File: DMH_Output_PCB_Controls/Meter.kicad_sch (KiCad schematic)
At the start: 63 parts, among them Q1 BC558, Q2 BC558, U1 TL072, U2 LM339, U3 LM339, U4 LM339, U5 LM339, U6 LM339

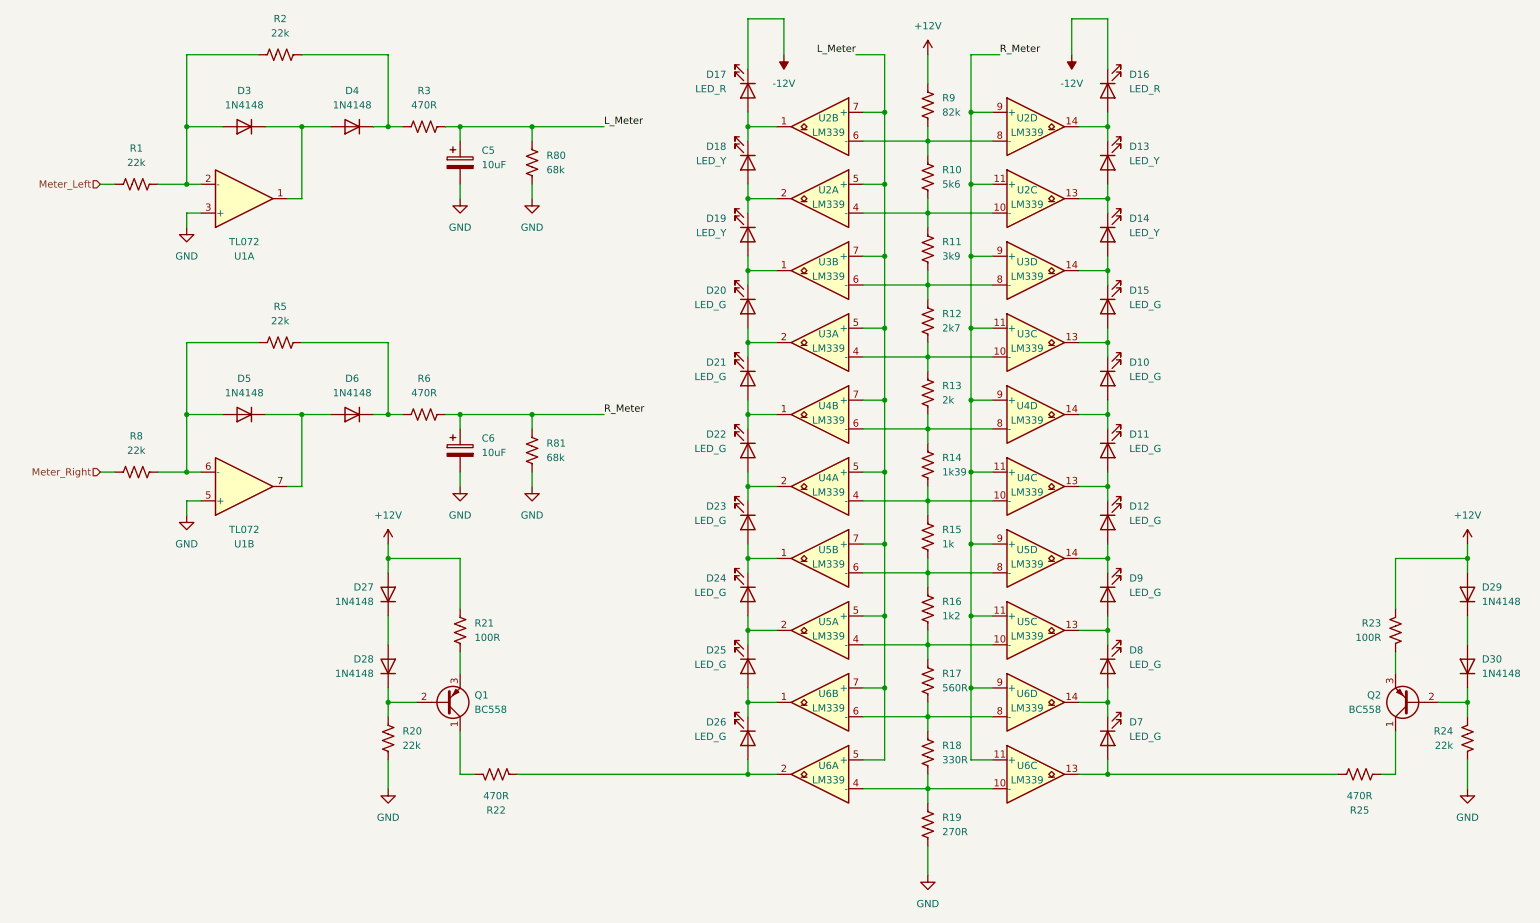
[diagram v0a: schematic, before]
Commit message: Starting design of Controls PCB
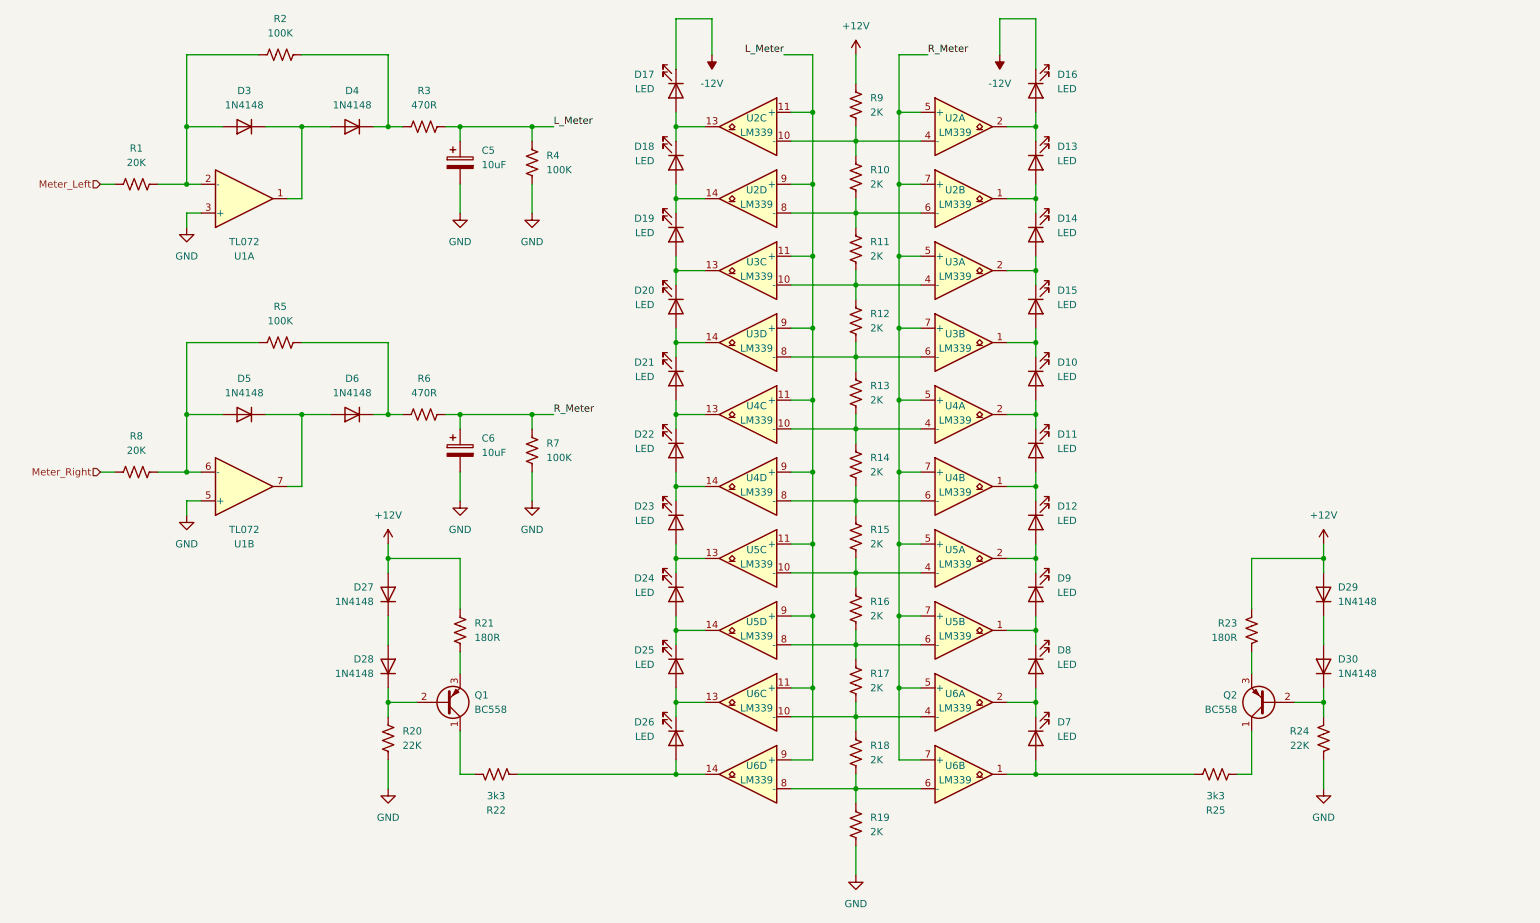
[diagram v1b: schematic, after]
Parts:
- removed R80: 68k, Resistor_THT:R_Axial_DIN0207_L6.3mm_D2.5mm_P7.62mm_Horizontal, symbol Device:R_US
- added R4: 100K, Resistor_THT:R_Axial_DIN0207_L6.3mm_D2.5mm_P7.62mm_Horizontal, symbol Device:R_US
- D10, D11, D12, D15, D20, D21, D22, D23, D24, D25, D26, D7, D8, D9: value LED_G -> LED
- D13, D14, D18, D19: value LED_Y -> LED
- D16, D17: value LED_R -> LED
- R1, R8: value 22k -> 20K
- R10: value 5k6 -> 2K
- R11: value 3k9 -> 2K
- R12: value 2k7 -> 2K
- R13: value 2k -> 2K
- R14: value 1k39 -> 2K
- R15: value 1k -> 2K
- R16: value 1k2 -> 2K
- R17: value 560R -> 2K
- R18: value 330R -> 2K
- R19: value 270R -> 2K
- R2, R5: value 22k -> 100K
- R20, R24: value 22k -> 22K
- R21, R23: value 100R -> 180R
- R22, R25: value 470R -> 3k3
- R7: renamed from R81; value 68k -> 100K
- R9: value 82k -> 2K
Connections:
- net GND: now also R4.1
- net L_Meter: now also U2.11 (+), U2.9 (+), U3.11 (+), U3.9 (+), U4.11 (+), U4.9 (+), U5.11 (+), U5.9 (+), U6.11 (+), U6.9 (+), R4.2; no longer U2.5 (+), U2.7 (+), U3.5 (+), U3.7 (+), U4.5 (+), U4.7 (+), U5.5 (+), U5.7 (+), U6.5 (+), U6.7 (+)
- net R_Meter: now also U2.5 (+), U2.7 (+), U3.5 (+), U3.7 (+), U4.5 (+), U4.7 (+), U5.5 (+), U5.7 (+), U6.5 (+), U6.7 (+); no longer U2.11 (+), U2.9 (+), U3.11 (+), U3.9 (+), U4.11 (+), U4.9 (+), U5.11 (+), U5.9 (+), U6.11 (+), U6.9 (+)
- net at D23.2 (A), D24.1 (K): now also U5.13; no longer U5.1
- net at U5.6 (-), U5.8 (-): now also R16.1, R17.2; no longer R15.1, R16.2
- net at D21.2 (A), D22.1 (K): now also U4.13; no longer U4.1
- net at U4.6 (-), U4.8 (-): now also R14.1, R15.2; no longer R13.1, R14.2
- net at U3.10 (-), U3.4 (-): now also R11.1, R12.2; no longer R12.1, R13.2
- net at D10.1 (K), D15.2 (A): now also U3.1; no longer U3.13
- net at D7.1 (K), D8.2 (A): now also U6.2; no longer U6.14
- net at D7.2 (A), R25.2: now also U6.1; no longer U6.13
- net at D24.2 (A), D25.1 (K): now also U5.14; no longer U5.2
- net at D19.2 (A), D20.1 (K): now also U3.13; no longer U3.1
- net at D20.2 (A), D21.1 (K): now also U3.14; no longer U3.2
- net at U3.6 (-), U3.8 (-): now also R12.1, R13.2; no longer R11.1, R12.2
- net at R10.1, R11.2: now also U2.6 (-), U2.8 (-); no longer U2.10 (-), U2.4 (-)
- net at D8.1 (K), D9.2 (A): now also U5.1; no longer U5.13
- net at D22.2 (A), D23.1 (K): now also U4.14; no longer U4.2
- net at U4.10 (-), U4.4 (-): now also R13.1, R14.2; no longer R14.1, R15.2
- net at D14.2 (A), D15.1 (K): now also U3.2; no longer U3.14
- net at D10.2 (A), D11.1 (K): now also U4.2; no longer U4.14
- net at D26.2 (A), R22.2: now also U6.14; no longer U6.2
- net at D13.1 (K), D16.2 (A): now also U2.2; no longer U2.14
- net at R10.2, R9.1: now also U2.10 (-), U2.4 (-); no longer U2.6 (-), U2.8 (-)
- net at R17.1, R18.2: now also U6.10 (-), U6.4 (-); no longer U6.6 (-), U6.8 (-)
- net at U5.10 (-), U5.4 (-): now also R15.1, R16.2; no longer R16.1, R17.2
- net at D25.2 (A), D26.1 (K): now also U6.13; no longer U6.1
- net at R18.1, R19.2: now also U6.6 (-), U6.8 (-); no longer U6.10 (-), U6.4 (-)
- net at D12.2 (A), D9.1 (K): now also U5.2; no longer U5.14
- net at D17.2 (A), D18.1 (K): now also U2.13; no longer U2.1
- net at D18.2 (A), D19.1 (K): now also U2.14; no longer U2.2
- net at D11.2 (A), D12.1 (K): now also U4.1; no longer U4.13
- net at D13.2 (A), D14.1 (K): now also U2.1; no longer U2.13
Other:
- moved on the sheet: D10, D11, D12, D13, D14, D15, D16, D17, D18, D19, D20, D21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
